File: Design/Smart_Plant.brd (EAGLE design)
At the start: 80 x 129.1 mm, 67 parts, among them IC1 AMS1117-3.3, IC2 TLC555CDR, IC3 AHT20, IC4 TP4056, J2 USBC-6P, Q1 IRLML0100, Q2 ALS-PT19-315C, T1 MMBT2222A, T2 LBSS84LT1G, U1 ESP-32S

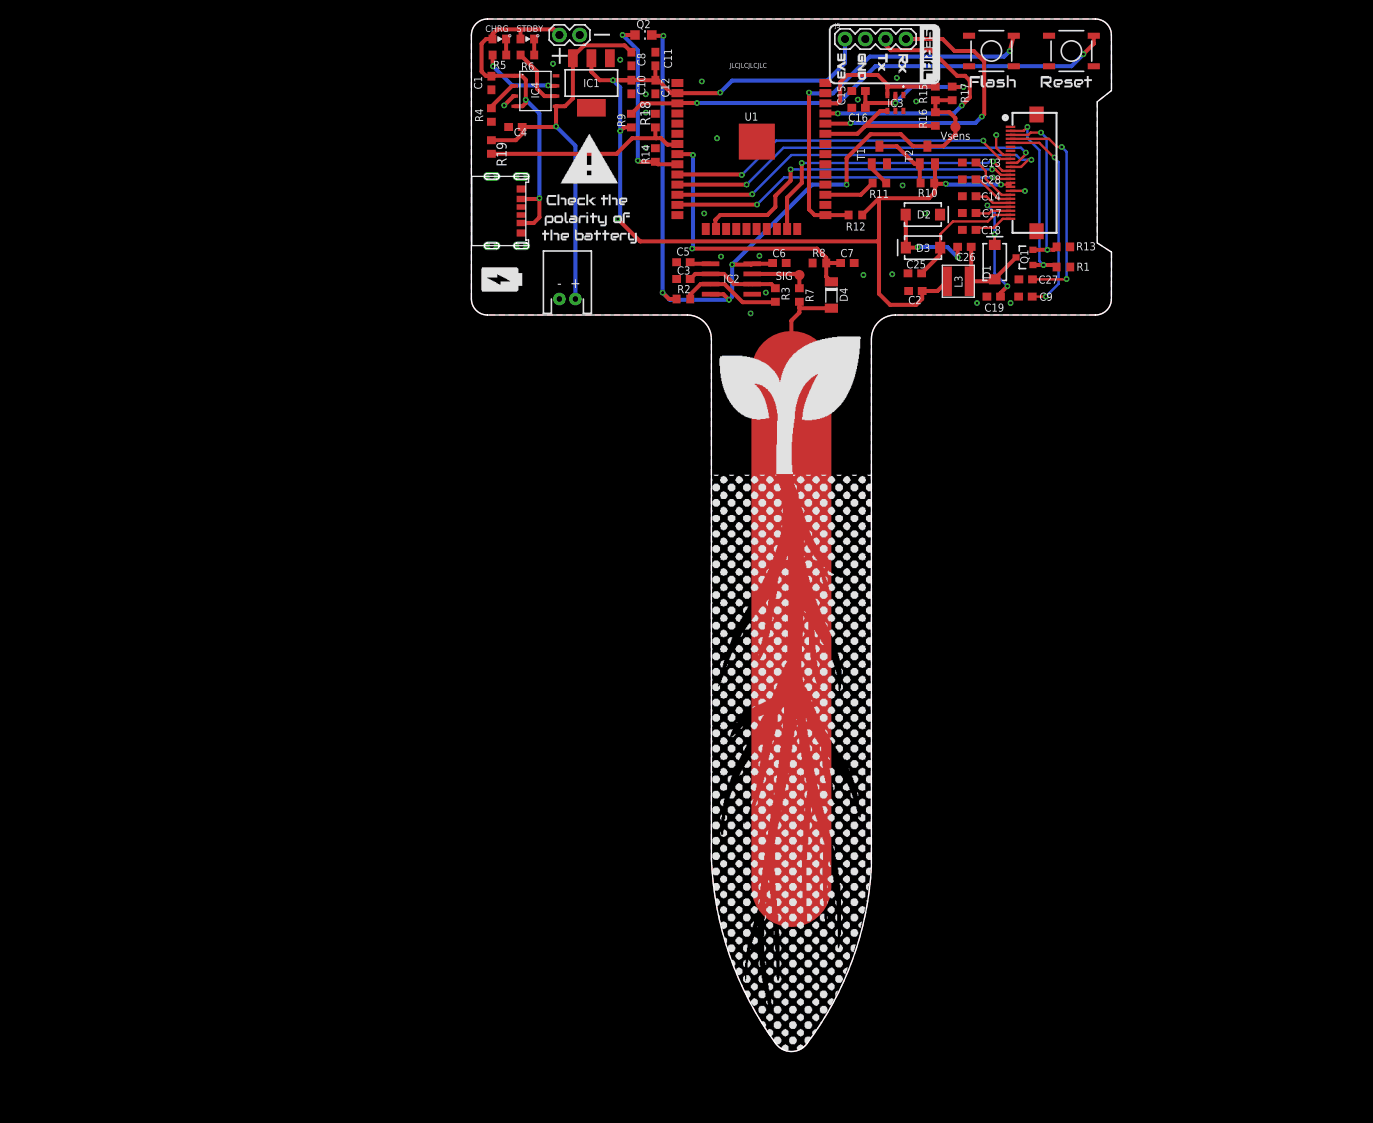
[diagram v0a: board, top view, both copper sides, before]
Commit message: Added power patch
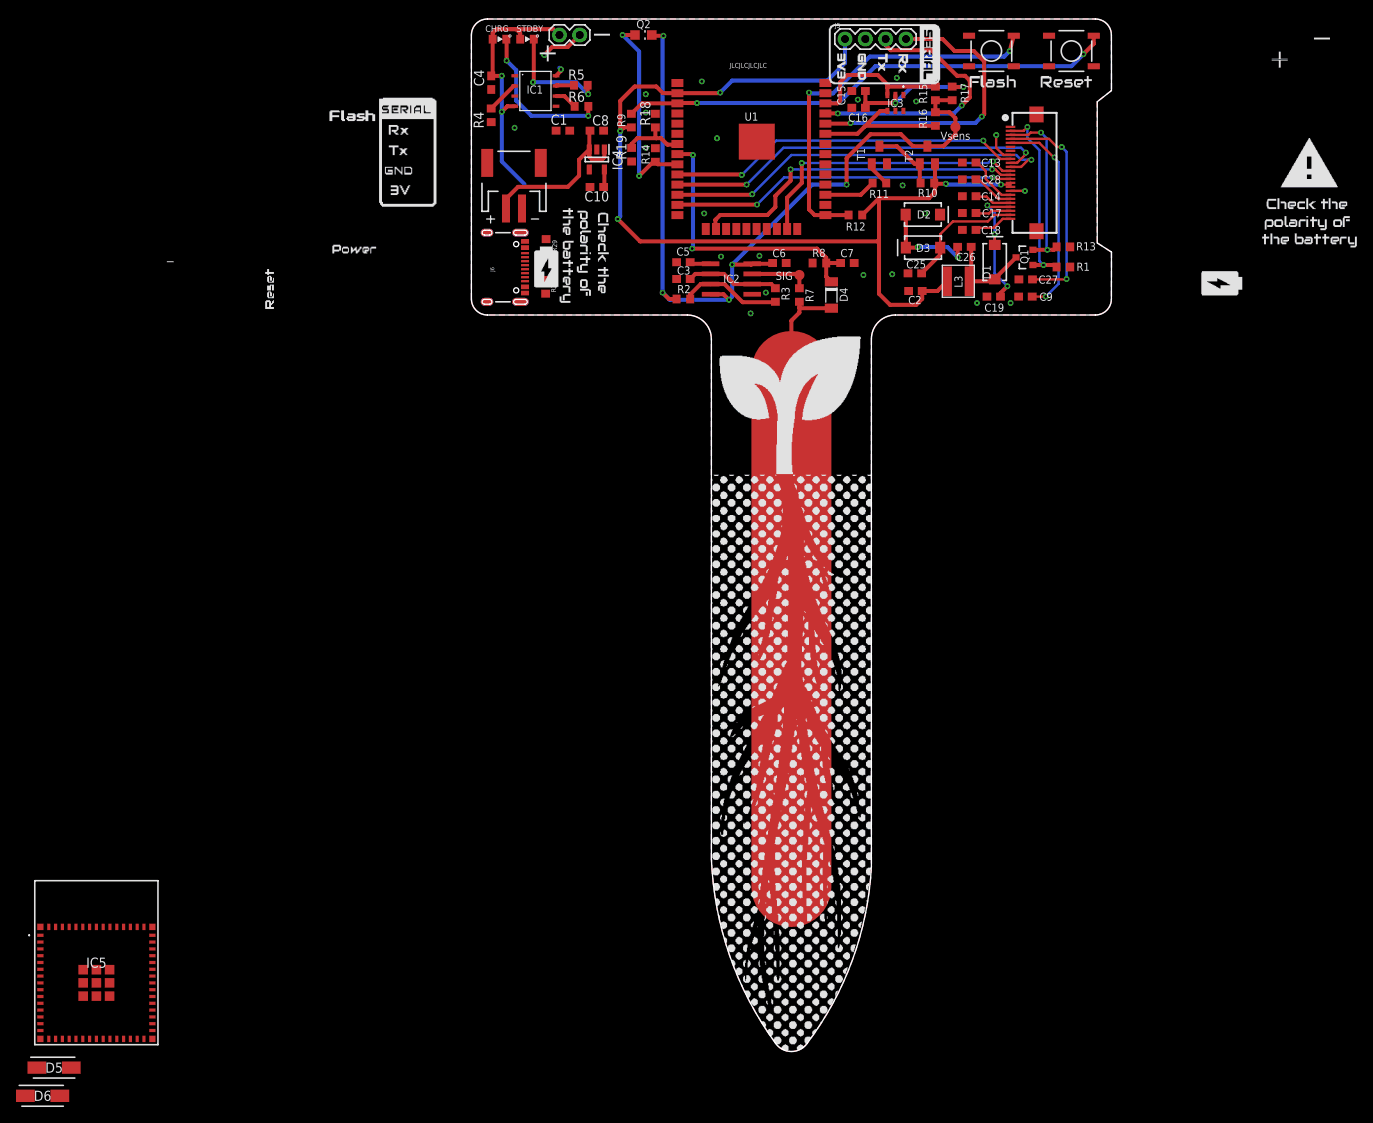
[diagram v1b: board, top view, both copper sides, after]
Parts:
- removed C11: 100nF, rcl:C0603
- removed C12: 22uF, rcl:C0603
- removed J2: USBC-6P, SpaceDIY_connectors:USCX-06FX-XXMX-01
- added D5, D6: B340A-13-F, SamacSys_Parts:DIOM5226X240N
- added IC5: ESP32-S3-MINI-1-N8, SamacSys_Parts:ESP32S3MINI1N8
- added J6: USB-C, SparkFun-Connectors:USB-C-16P-4LAYER-ISOLATED
- added R28, R29: 5.1k, rcl:R0603
- IC1: value AMS1117-3.3 -> TP4056; device SparkFun-IC-Power:SOT223 -> TP4056:SOT23-8
- IC4: value TP4056 -> RT9080-33GJ5; device TP4056:SOT23-8 -> SamacSys_Parts:SOT94P280X100-5N
- J4: device SparkFun-Connectors:JST-2-PTH-NS -> SpaceDIY_connectors:JST-2-SMD
- moved R19 17.5 mm to (20.0, 20.0), turned to 90 degrees
- moved J4 16.7 mm to (5.32, 17.3), turned to 180 degrees
- moved C10 13.2 mm to (15.7, 16.0), turned to 180 degrees
- moved IC4 11.5 mm to (15.7, 19.4)
- moved R5 10.9 mm to (13.7, 28.7)
- moved C1 10.7 mm to (11.4, 23.0), turned to 0 degrees
- moved C8 9.95 mm to (15.7, 23.0), turned to 0 degrees
- moved R6 9.32 mm to (13.8, 26.1)
- moved IC1 7.07 mm to (8.00, 28.0), turned to 270 degrees
- moved C4 6.31 mm to (2.48, 29.0), turned to 270 degrees
- moved LED2 3.48 mm to (3.52, 34.5)
- moved LED1 3.46 mm to (6.96, 34.5)
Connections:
- removed net N$2 (its old number): IC4.6, R6.2
- new net CC1: J6.B5, R28.2
- new net CC2: J6.A5, R29.2
- new net D+: J6.A6, J6.B6
- new net D-: J6.A7, J6.B7
- new net N$35: D6.2, J1.1
- new net N$4: IC1.2, R4.2
- new net V_USB: D5.2, J6.VBUS1, J6.VBUS2
- net 3.3V: now also IC4.5, IC5.3; no longer C11.1, C12.1, IC1.2
- net BATTERY: now also IC5.31
- net GND: now also IC1.3, IC4.2, IC5.1, IC5.2, IC5.42, IC5.43, IC5.46, IC5.47, IC5.48, IC5.49, IC5.50, IC5.51, IC5.52, IC5.53, IC5.54, IC5.55, IC5.56, IC5.57, IC5.58, IC5.59, IC5.60, IC5.61, IC5.62, IC5.63, IC5.64, IC5.65, IC5.66, IC5.67, IC5.68, IC5.69, IC5.70, IC5.71, IC5.72, IC5.73, J4.2, J6.GND, J6.GND2, R28.1, R29.1; no longer C11.2, C12.2, IC4.3, IC4.8, J2.GND1, J2.GND2, J4.1
- net N$1: now also IC1.6, R6.2; no longer IC4.2, R4.2
- net N$6: now also IC1.7; no longer IC4.7
- net RST: now also IC5.45
- net VBAT: now also C1.1, IC1.5, IC4.1, IC4.3, J4.1; no longer C4.1, IC1.3, IC4.5, J4.2
- net VIN: now also C4.1, D5.1, D6.1, IC1.4, IC1.8; no longer C1.1, IC4.1, IC4.4, J1.1, J2.VBUS1, J2.VBUS2
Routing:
- net VBAT: track 50.4 -> 21.8 mm, vias 1 -> 0
- net BATTERY: track 25.8 -> 8.27 mm
- net N$3: track 2.00 -> 19.2 mm, vias 0 -> 2
- net VIN: track 46.9 -> 34.7 mm, vias 2 -> 3
- net N$2: track 2.00 -> 14.1 mm, vias 0 -> 2
- net 3.3V: track 142.9 -> 133.2 mm, vias 6 -> 5
- net N$6: track 10.3 -> 2.29 mm, vias 2 -> 0
- net N$2 (its old number): track 7.82 -> 0.00 mm
- net N$4: track 0.00 -> 4.11 mm
- net GND: track 7.38 -> 11.0 mm, vias 24 -> 23
- net LIGHT: track 23.2 -> 25.7 mm
- net N$1: track 4.19 -> 2.86 mm

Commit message: Released designs from V1R1 with the patch board
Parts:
- removed D5, D6: B340A-13-F, SamacSys_Parts:DIOM5226X240N
- removed IC5: ESP32-S3-MINI-1-N8, SamacSys_Parts:ESP32S3MINI1N8
- removed J6: USB-C, SparkFun-Connectors:USB-C-16P-4LAYER-ISOLATED
- removed R28, R29: 5.1k, rcl:R0603
- added C11: 100nF, rcl:C0603
- added C12: 22uF, rcl:C0603
- added J2: USBC-6P, SpaceDIY_connectors:USCX-06FX-XXMX-01
- IC1: value TP4056 -> AMS1117-3.3; device TP4056:SOT23-8 -> SparkFun-IC-Power:SOT223
- IC4: value RT9080-33GJ5 -> TP4056; device SamacSys_Parts:SOT94P280X100-5N -> TP4056:SOT23-8
- J4: device SpaceDIY_connectors:JST-2-SMD -> SparkFun-Connectors:JST-2-PTH-NS
- moved R19 17.5 mm to (2.50, 21.0), turned to 270 degrees
- moved J4 16.7 mm to (12.0, 2.00), turned to 0 degrees
- moved C10 13.2 mm to (20.0, 28.5), turned to 270 degrees
- moved IC4 11.5 mm to (8.00, 28.0)
- moved R5 10.9 mm to (3.50, 32.5)
- moved C1 10.7 mm to (2.50, 29.0), turned to 270 degrees
- moved C8 9.95 mm to (20.0, 32.0), turned to 270 degrees
- moved R6 9.32 mm to (7.00, 32.5)
- moved IC1 7.07 mm to (15.0, 29.0), turned to 180 degrees
- moved C4 6.31 mm to (5.50, 23.5), turned to 180 degrees
- moved LED2 3.48 mm to (7.00, 34.5)
- moved LED1 3.46 mm to (3.50, 34.5)
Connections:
- removed net CC1: J6.B5, R28.2
- removed net CC2: J6.A5, R29.2
- removed net D+: J6.A6, J6.B6
- removed net D-: J6.A7, J6.B7
- removed net N$35: D6.2, J1.1
- removed net N$4 (its old number): IC1.2, R4.2
- removed net V_USB: D5.2, J6.VBUS1, J6.VBUS2
- new net N$2: IC4.6, R6.2
- net 3.3V: now also C11.1, C12.1, IC1.2; no longer IC4.5, IC5.3
- net BATTERY: no longer IC5.31
- net GND: now also C11.2, C12.2, IC4.3, IC4.8, J2.GND1, J2.GND2, J4.1; no longer IC1.3, IC4.2, IC5.1, IC5.2, IC5.42, IC5.43, IC5.46, IC5.47, IC5.48, IC5.49, IC5.50, IC5.51, IC5.52, IC5.53, IC5.54, IC5.55, IC5.56, IC5.57, IC5.58, IC5.59, IC5.60, IC5.61, IC5.62, IC5.63, IC5.64, IC5.65, IC5.66, IC5.67, IC5.68, IC5.69, IC5.70, IC5.71, IC5.72, IC5.73, J4.2, J6.GND, J6.GND2, R28.1, R29.1
- net N$1: now also IC4.2, R4.2; no longer IC1.6, R6.2
- net N$6: now also IC4.7; no longer IC1.7
- net RST: no longer IC5.45
- net VBAT: now also C4.1, IC1.3, IC4.5, J4.2; no longer C1.1, IC1.5, IC4.1, IC4.3, J4.1
- net VIN: now also C1.1, IC4.1, IC4.4, J1.1, J2.VBUS1, J2.VBUS2; no longer C4.1, D5.1, D6.1, IC1.4, IC1.8
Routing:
- net VBAT: track 21.8 -> 50.4 mm, vias 0 -> 1
- net BATTERY: track 8.27 -> 25.8 mm
- net N$4: track 19.2 -> 2.00 mm, vias 2 -> 0
- net VIN: track 34.7 -> 46.9 mm, vias 3 -> 2
- net N$3: track 14.1 -> 2.00 mm, vias 2 -> 0
- net 3.3V: track 133.2 -> 142.9 mm, vias 5 -> 6
- net N$6: track 2.29 -> 10.3 mm, vias 0 -> 2
- net N$2: track 0.00 -> 7.82 mm
- net N$4 (its old number): track 4.11 -> 0.00 mm
- net GND: track 11.0 -> 7.38 mm, vias 23 -> 24
- net LIGHT: track 25.7 -> 23.2 mm
- net N$1: track 2.86 -> 4.19 mm
